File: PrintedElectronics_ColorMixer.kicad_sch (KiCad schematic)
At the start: 5 parts

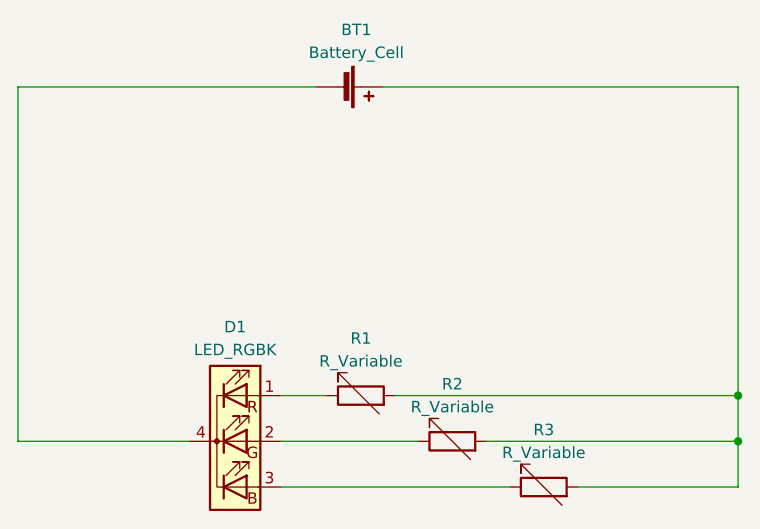
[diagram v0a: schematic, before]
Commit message: coarser humditiy sensor and bridges for stencils
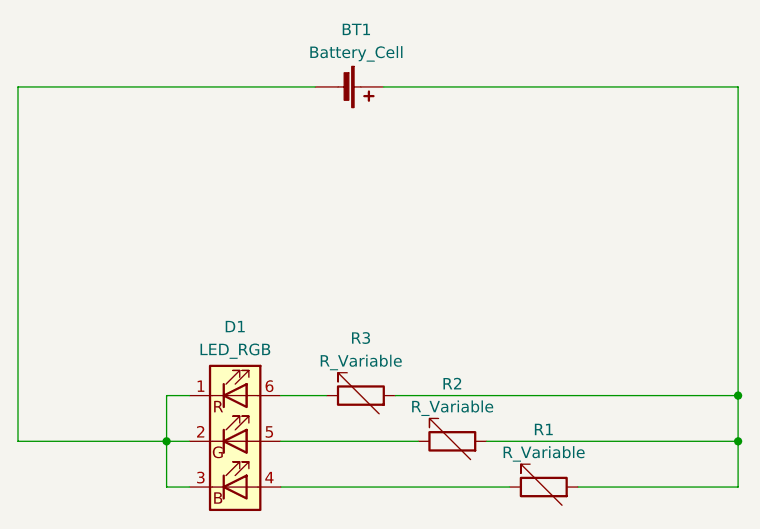
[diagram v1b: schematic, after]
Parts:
- removed D1: LED_RGBK, LED_SMD:LED_RGB_5050-6, symbol Device:LED_RGBK
- added D1: LED_RGB, LED_SMD:LED_RGB_5050-6, symbol Device:LED_RGB
- R1, R2, R3: footprint CHAIR:Humidity_Sensor_Printed_Electronics -> CHAIR:Humidity_Sensor_Printed_Electronics_Stencil
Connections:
- net at R1.1: now also D1.4 (BA)
- net at R2.1: now also D1.5 (GA)
- net at R3.1: now also D1.6 (RA)
- net at BT1.2 (-): now also D1.1 (RK), D1.2 (GK), D1.3 (BK)
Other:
- moved on the sheet: R1, R3
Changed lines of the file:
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@@
 (kicad_sch (version 20230121) (generator eeschema)
   (paper "A4")
+  (junction (at 109.22 102.87) (diameter 0) (color 0 0 0 0)
+  )
   (junction (at 172.72 97.79) (diameter 0) (color 0 0 0 0)
   )
@@
   )
   (wire (pts (xy 92.71 63.5) (xy 125.73 63.5))
+    (stroke (width 0) (type default))
+  )
+  (wire (pts (xy 111.76 97.79) (xy 109.22 97.79))
+    (stroke (width 0) (type default))
+  )
+  (wire (pts (xy 109.22 97.79) (xy 109.22 102.87))
+    (stroke (width 0) (type default))
+  )
+  (wire (pts (xy 111.76 107.95) (xy 109.22 107.95))
     (stroke (width 0) (type default))
   )
@@
     (stroke (width 0) (type default))
   )
+  (wire (pts (xy 109.22 107.95) (xy 109.22 102.87))
+    (stroke (width 0) (type default))
+  )
   (wire (pts (xy 172.72 63.5) (xy 172.72 97.79))
+    (stroke (width 0) (type default))
+  )
+  (wire (pts (xy 109.22 102.87) (xy 92.71 102.87))
     (stroke (width 0) (type default))
   )
@@
     (stroke (width 0) (type default))
   )
-  (wire (pts (xy 111.76 102.87) (xy 92.71 102.87))
+  (wire (pts (xy 111.76 102.87) (xy 109.22 102.87))
     (stroke (width 0) (type default))
   )
-  (symbol (lib_id "Device:LED_RGBK") (at 116.84 102.87 0) (unit 1)
+  (symbol (lib_id "Device:R_Variable") (at 151.13 107.95 90) (unit 1)
     (in_bom yes) (on_board yes) (dnp no) (fields_autoplaced)
-    (property "Reference" "D1" (at 116.84 90.17 0)
+    (property "Reference" "R1" (at 151.13 101.6 90)
       (effects (font (size 1.27 1.27)))
     )
-    (property "Value" "LED_RGBK" (at 116.84 92.71 0)
+    (property "Value" "R_Variable" (at 151.13 104.14 90)
       (effects (font (size 1.27 1.27)))
     )
-    (property "Footprint" "LED_SMD:LED_RGB_5050-6" (at 116.84 104.14 0)
+    (property "Footprint" "CHAIR:Humidity_Sensor_Printed_Electronics_Stencil" (at 151.13 109.728 90)
       (effects (font (size 1.27 1.27)) hide)
     )
-    (property "Datasheet" "~" (at 116.84 104.14 0)
+    (property "Datasheet" "~" (at 151.13 107.95 0)
       (effects (font (size 1.27 1.27)) hide)
     )
     (pin "1")
     (pin "2")
-    (pin "3")
-    (pin "4")
     (instances
-      (project "absolute_beginner"
+      (project "PrintedElectronics_ColorMixer"
         (path "/78b14467-0f38-4cbf-9bf4-49acfbe55300"
-          (reference "D1") (unit 1)
+          (reference "R1") (unit 1)
         )
       )
@@
   (symbol (lib_id "Device:R_Variable") (at 130.81 97.79 90) (unit 1)
     (in_bom yes) (on_board yes) (dnp no) (fields_autoplaced)
-    (property "Reference" "R1" (at 130.81 91.44 90)
+    (property "Reference" "R3" (at 130.81 91.44 90)
       (effects (font (size 1.27 1.27)))
     )
@@
       (effects (font (size 1.27 1.27)))
     )
-    (property "Footprint" "CHAIR:Humidity_Sensor_Printed_Electronics" (at 130.81 99.568 90)
+    (property "Footprint" "CHAIR:Humidity_Sensor_Printed_Electronics_Stencil" (at 130.81 99.568 90)
       (effects (font (size 1.27 1.27)) hide)
     )
@@
     (pin "2")
     (instances
-      (project "absolute_beginner"
-        (path "/78b14467-0f38-4cbf-9bf4-49acfbe55300"
-          (reference "R1") (unit 1)
-        )
-      )
-    )
-  )
-  (symbol (lib_id "Device:R_Variable") (at 151.13 107.95 90) (unit 1)
-    (in_bom yes) (on_board yes) (dnp no) (fields_autoplaced)
-    (property "Reference" "R3" (at 151.13 101.6 90)
-      (effects (font (size 1.27 1.27)))
-    )
-    (property "Value" "R_Variable" (at 151.13 104.14 90)
-      (effects (font (size 1.27 1.27)))
-    )
-    (property "Footprint" "CHAIR:Humidity_Sensor_Printed_Electronics" (at 151.13 109.728 90)
-      (effects (font (size 1.27 1.27)) hide)
-    )
-    (property "Datasheet" "~" (at 151.13 107.95 0)
-      (effects (font (size 1.27 1.27)) hide)
-    )
-    (pin "1")
-    (pin "2")
-    (instances
-      (project "absolute_beginner"
+      (project "PrintedElectronics_ColorMixer"
         (path "/78b14467-0f38-4cbf-9bf4-49acfbe55300"
           (reference "R3") (unit 1)
@@
     (pin "2")
     (instances
-      (project "absolute_beginner"
+      (project "PrintedElectronics_ColorMixer"
         (path "/78b14467-0f38-4cbf-9bf4-49acfbe55300"
           (reference "BT1") (unit 1)
@@
       (effects (font (size 1.27 1.27)))
     )
-    (property "Footprint" "CHAIR:Humidity_Sensor_Printed_Electronics" (at 140.97 104.648 90)
+    (property "Footprint" "CHAIR:Humidity_Sensor_Printed_Electronics_Stencil" (at 140.97 104.648 90)
       (effects (font (size 1.27 1.27)) hide)
     )
@@
     (pin "2")
     (instances
-      (project "absolute_beginner"
+      (project "PrintedElectronics_ColorMixer"
         (path "/78b14467-0f38-4cbf-9bf4-49acfbe55300"
           (reference "R2") (unit 1)
         )
       )
+    )
+  )
+  (symbol (lib_id "Device:LED_RGB") (at 116.84 102.87 0) (unit 1)
+    (in_bom yes) (on_board yes) (dnp no) (fields_autoplaced)
+    (property "Reference" "D1" (at 116.84 90.17 0)
+      (effects (font (size 1.27 1.27)))
+    )
+    (property "Value" "LED_RGB" (at 116.84 92.71 0)
+      (effects (font (size 1.27 1.27)))
+    )
+    (property "Footprint" "LED_SMD:LED_RGB_5050-6" (at 116.84 104.14 0)
+      (effects (font (size 1.27 1.27)) hide)
+    )
+    (property "Datasheet" "~" (at 116.84 104.14 0)
+      (effects (font (size 1.27 1.27)) hide)
+    )
+    (pin "2")
+    (pin "5")
+    (pin "4")
+    (pin "1")
+    (pin "6")
+    (pin "3")
+    (instances
+      (project "PrintedElectronics_ColorMixer"
+        (path "/78b14467-0f38-4cbf-9bf4-49acfbe55300"
+          (reference "D1") (unit 1)
+        )
+      )
